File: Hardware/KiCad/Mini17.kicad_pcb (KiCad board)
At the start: 2 copper layers, 160 parts, among them IC1 LM4861M, J1 USB_C, J2 STLink, J3 Micro_SD_Card_Det, J6 UART, J7 OLED, J8 Conn_Coaxial, SW1 PTT, SW10 SW_Push_45deg, SW11 SW_Push_45deg, SW12 SW_Push_45deg, SW13 SW_Push_45deg, SW14 SW_Push_45deg, SW15 SW_Push_45deg, SW16 SW_Push_45deg, SW17 SW_Push_45deg, SW2 SW_Push_45deg, SW3 SW_Push_45deg, SW4 SW_Push_45deg, SW5 SW_Push_45deg, SW6 SW_Push_45deg, SW7 SW_Push_45deg, SW8 SW_Push_45deg, SW9 SW_Push_45deg, U1 USBLC6-2, U3 STM32F427ZGTx, U4 CC1200, U5 MAX9814, U6 TP6841S6, U7 TPS73233, Y1 8 MHz, Y3 40 MHz

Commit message: move cc1200 spi to spi-5 & update other labels throughout
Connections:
- U3 pad 110: CC_NCS -> unconnected-(U3-Pad110)
- U3 pad 133: CC_SCLK -> unconnected-(U3-Pad133)
- U3 pad 134: CC_MISO -> unconnected-(U3-Pad134)
- U3 pad 135: CC_MOSI -> unconnected-(U3-Pad135)
- U3 pad 137: CC_NRST -> unconnected-(U3-Pad137)
- U3 pad 15: unconnected-(U3-Pad15) -> CC_NRST
- U3 pad 18: unconnected-(U3-Pad18) -> CC_NCS
- U3 pad 19: unconnected-(U3-Pad19) -> CC_SCLK
- U3 pad 20: unconnected-(U3-Pad20) -> CC_MISO
- U3 pad 21: unconnected-(U3-Pad21) -> CC_MOSI
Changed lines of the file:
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@@
   (net 119 "unconnected-(U3-Pad13)")
   (net 120 "unconnected-(U3-Pad14)")
-  (net 121 "unconnected-(U3-Pad15)")
-  (net 122 "unconnected-(U3-Pad18)")
-  (net 123 "unconnected-(U3-Pad19)")
-  (net 124 "unconnected-(U3-Pad20)")
-  (net 125 "unconnected-(U3-Pad21)")
+  (net 121 "unconnected-(U3-Pad110)")
+  (net 122 "unconnected-(U3-Pad133)")
+  (net 123 "unconnected-(U3-Pad134)")
+  (net 124 "unconnected-(U3-Pad135)")
+  (net 125 "unconnected-(U3-Pad137)")
   (net 126 "unconnected-(U3-Pad22)")
   (net 127 "unconnected-(U3-Pad26)")
@@
       (net 120 "unconnected-(U3-Pad14)") (pinfunction "PF4") (pintype "bidirectional"))
     (pad "15" smd roundrect (at -10.6625 -1.75) (size 1.475 0.3) (layers "F.Cu" "F.Paste" "F.Mask") (roundrect_rratio 0.25)
-      (net 121 "unconnected-(U3-Pad15)") (pinfunction "PF5") (pintype "bidirectional"))
+      (net 186 "CC_NRST") (pinfunction "PF5") (pintype "bidirectional"))
     (pad "16" smd roundrect (at -10.6625 -1.25) (size 1.475 0.3) (layers "F.Cu" "F.Paste" "F.Mask") (roundrect_rratio 0.25)
       (net 1 "GND") (pinfunction "VSS") (pintype "power_in"))
@@
       (net 20 "VDD") (pinfunction "VDD") (pintype "power_in"))
     (pad "18" smd roundrect (at -10.6625 -0.25) (size 1.475 0.3) (layers "F.Cu" "F.Paste" "F.Mask") (roundrect_rratio 0.25)
-      (net 122 "unconnected-(U3-Pad18)") (pinfunction "PF6") (pintype "bidirectional"))
+      (net 167 "CC_NCS") (pinfunction "PF6") (pintype "bidirectional"))
     (pad "19" smd roundrect (at -10.6625 0.25) (size 1.475 0.3) (layers "F.Cu" "F.Paste" "F.Mask") (roundrect_rratio 0.25)
-      (net 123 "unconnected-(U3-Pad19)") (pinfunction "PF7") (pintype "bidirectional"))
+      (net 182 "CC_SCLK") (pinfunction "PF7") (pintype "bidirectional"))
     (pad "20" smd roundrect (at -10.6625 0.75) (size 1.475 0.3) (layers "F.Cu" "F.Paste" "F.Mask") (roundrect_rratio 0.25)
-      (net 124 "unconnected-(U3-Pad20)") (pinfunction "PF8") (pintype "bidirectional"))
+      (net 183 "CC_MISO") (pinfunction "PF8") (pintype "bidirectional"))
     (pad "21" smd roundrect (at -10.6625 1.25) (size 1.475 0.3) (layers "F.Cu" "F.Paste" "F.Mask") (roundrect_rratio 0.25)
-      (net 125 "unconnected-(U3-Pad21)") (pinfunction "PF9") (pintype "bidirectional"))
+      (net 184 "CC_MOSI") (pinfunction "PF9") (pintype "bidirectional"))
     (pad "22" smd roundrect (at -10.6625 1.75) (size 1.475 0.3) (layers "F.Cu" "F.Paste" "F.Mask") (roundrect_rratio 0.25)
       (net 126 "unconnected-(U3-Pad22)") (pinfunction "PF10") (pintype "bidirectional"))
@@
       (net 74 "SWCLK") (pinfunction "PA14") (pintype "bidirectional"))
     (pad "110" smd roundrect (at 8.25 -10.6625) (size 0.3 1.475) (layers "F.Cu" "F.Paste" "F.Mask") (roundrect_rratio 0.25)
-      (net 167 "CC_NCS") (pinfunction "PA15") (pintype "bidirectional"))
+      (net 121 "unconnected-(U3-Pad110)") (pinfunction "PA15") (pintype "bidirectional"))
     (pad "111" smd roundrect (at 7.75 -10.6625) (size 0.3 1.475) (layers "F.Cu" "F.Paste" "F.Mask") (roundrect_rratio 0.25)
       (net 59 "SD_D2") (pinfunction "PC10") (pintype "bidirectional"))
@@
       (net 181 "unconnected-(U3-Pad132)") (pinfunction "PG15") (pintype "bidirectional"))
     (pad "133" smd roundrect (at -3.25 -10.6625) (size 0.3 1.475) (layers "F.Cu" "F.Paste" "F.Mask") (roundrect_rratio 0.25)
-      (net 182 "CC_SCLK") (pinfunction "PB3") (pintype "bidirectional"))
+      (net 122 "unconnected-(U3-Pad133)") (pinfunction "PB3") (pintype "bidirectional"))
     (pad "134" smd roundrect (at -3.75 -10.6625) (size 0.3 1.475) (layers "F.Cu" "F.Paste" "F.Mask") (roundrect_rratio 0.25)
-      (net 183 "CC_MISO") (pinfunction "PB4") (pintype "bidirectional"))
+      (net 123 "unconnected-(U3-Pad134)") (pinfunction "PB4") (pintype "bidirectional"))
     (pad "135" smd roundrect (at -4.25 -10.6625) (size 0.3 1.475) (layers "F.Cu" "F.Paste" "F.Mask") (roundrect_rratio 0.25)
-      (net 184 "CC_MOSI") (pinfunction "PB5") (pintype "bidirectional"))
+      (net 124 "unconnected-(U3-Pad135)") (pinfunction "PB5") (pintype "bidirectional"))
     (pad "136" smd roundrect (at -4.75 -10.6625) (size 0.3 1.475) (layers "F.Cu" "F.Paste" "F.Mask") (roundrect_rratio 0.25)
       (net 185 "unconnected-(U3-Pad136)") (pinfunction "PB6") (pintype "bidirectional"))
     (pad "137" smd roundrect (at -5.25 -10.6625) (size 0.3 1.475) (layers "F.Cu" "F.Paste" "F.Mask") (roundrect_rratio 0.25)
-      (net 186 "CC_NRST") (pinfunction "PB7") (pintype "bidirectional"))
+      (net 125 "unconnected-(U3-Pad137)") (pinfunction "PB7") (pintype "bidirectional"))
     (pad "138" smd roundrect (at -5.75 -10.6625) (size 0.3 1.475) (layers "F.Cu" "F.Paste" "F.Mask") (roundrect_rratio 0.25)
       (net 187 "~{BOOT0}") (pinfunction "BOOT0") (pintype "input"))

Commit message: starting basic layout
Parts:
- moved J8 118.1 mm to (278.1, 117.0), turned to -90 degrees
- moved H2 106.7 mm to (143.1, 175.0)
- moved H1 106.7 mm to (141.4, 180.4)
- moved H3 106.7 mm to (151.3, 167.1)
- moved H4 106.7 mm to (135.8, 183.3)
- moved J3 105.8 mm to (66.3, 188.9)
- moved C51 105.2 mm to (267.7, 118.0), turned to 180 degrees
- moved C54 103.8 mm to (272.2, 118.4), turned to -90 degrees
- moved R29 103.2 mm to (265.2, 120.2), turned to 90 degrees
- moved L9 100.6 mm to (272.6, 117.0)
- moved L8 99.7 mm to (270.7, 117.0)
- moved L7 99.4 mm to (267.7, 117.0)
- moved L6 99.0 mm to (264.2, 117.5), turned to 90 degrees
- moved C50 95.9 mm to (264.2, 120.1), turned to 90 degrees
- moved C27 95.1 mm to (220.9, 36.9)
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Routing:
- net CC_X1: track 0.00 -> 9.32 mm
- net CC_X2: track 0.00 -> 6.42 mm
- net GND: track 0.00 -> 3.70 mm

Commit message: rough layout of cc1200
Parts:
- added C11: 47n, Capacitor_SMD:C_0402_1005Metric, F.Cu at (238.9, 113.0)
- added C121: 47n, Capacitor_SMD:C_0402_1005Metric, F.Cu at (243.7, 121.3)
- added C131: 47n, Capacitor_SMD:C_0402_1005Metric, F.Cu at (244.8, 121.3)
- added C151: 47n, Capacitor_SMD:C_0402_1005Metric, F.Cu at (245.9, 120.2)
- added C221: 47n, Capacitor_SMD:C_0402_1005Metric, F.Cu at (251.3, 112.4)
- added C251: 47n, Capacitor_SMD:C_0402_1005Metric, F.Cu at (248.1, 109.5)
- added C271: 47n, Capacitor_SMD:C_0402_1005Metric, F.Cu at (246.1, 109.5)
- added C281: 47n, Capacitor_SMD:C_0402_1005Metric, F.Cu at (245.0, 109.5)
- added C51: 47n, Capacitor_SMD:C_0402_1005Metric, F.Cu at (238.9, 115.0)
- moved R171 16.8 mm to (248.5, 119.0), turned to 0 degrees
- moved L172 14.7 mm to (253.0, 116.5), turned to 90 degrees
- moved C174 14.2 mm to (251.5, 117.0)
- moved L171 14.2 mm to (250.0, 117.5), turned to -90 degrees
- moved C173 14.2 mm to (250.1, 119.5)
- moved C176 13.2 mm to (254.5, 117.0)
- moved C175 13.2 mm to (259.0, 117.4)
- moved C181 13.2 mm to (256.0, 116.6)
- moved L173 13.2 mm to (257.5, 117.0)
- moved L174 12.1 mm to (260.5, 117.0)
- moved J8 11.6 mm to (266.5, 117.0)
- moved C172 6.15 mm to (248.0, 120.5), turned to -90 degrees
- moved C301 3.48 mm to (241.3, 107.5), turned to 0 degrees
- moved L192 3.11 mm to (256.4, 113.1), turned to 0 degrees
- moved C291 2.86 mm to (244.1, 108.5), turned to -90 degrees
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- renumbered C52 to C171, C55 to C172, C50 to C173, C49 to C174, C54 to C175, C51 to C176, C53 to C181, C47 to C191, C48 to C201, C13 to C211, C10 to C231, C12 to C261, C11 to C291, C8 to C301, C9 to C311, C14 to C61, C61 to C9, L6 to L171, L7 to L172, L8 to L173, L9 to L174, L3 to L191, L2 to L192, L5 to L193, L4 to L201, R9 to R141, R29 to R171
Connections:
- C173 pad 2: Net-(C50-Pad2) -> Net-(C173-Pad2)
- L171 pad 1: Net-(C50-Pad2) -> PA
- L171 pad 2: PA -> Net-(C173-Pad2)
- R171 pad 2: Net-(C50-Pad2) -> Net-(C173-Pad2)
- U3 pad 6: +BATT -> VBAT
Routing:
- net VDD: track 0.00 -> 31.6 mm
- net GND: track 3.70 -> 20.9 mm
- net LNA_N: track 0.00 -> 10.2 mm
- net TRX_SW: track 0.00 -> 9.83 mm
- net LNA_P: track 0.00 -> 9.73 mm
- net CC_X1: track 9.32 -> 0.00 mm
- net Net-(C191-Pad2): track 0.00 -> 7.65 mm
- net CC_X2: track 6.42 -> 0.00 mm
- net Net-(J8-Pad1): track 0.00 -> 5.53 mm
- net Net-(C176-Pad1): track 0.00 -> 4.71 mm
- net Net-(C211-Pad1): track 0.00 -> 3.66 mm
- net Net-(C61-Pad1): track 0.00 -> 3.63 mm
- net Net-(C231-Pad2): track 0.00 -> 3.19 mm
- net PA: track 0.00 -> 3.17 mm
- net Net-(C261-Pad1): track 0.00 -> 3.01 mm
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
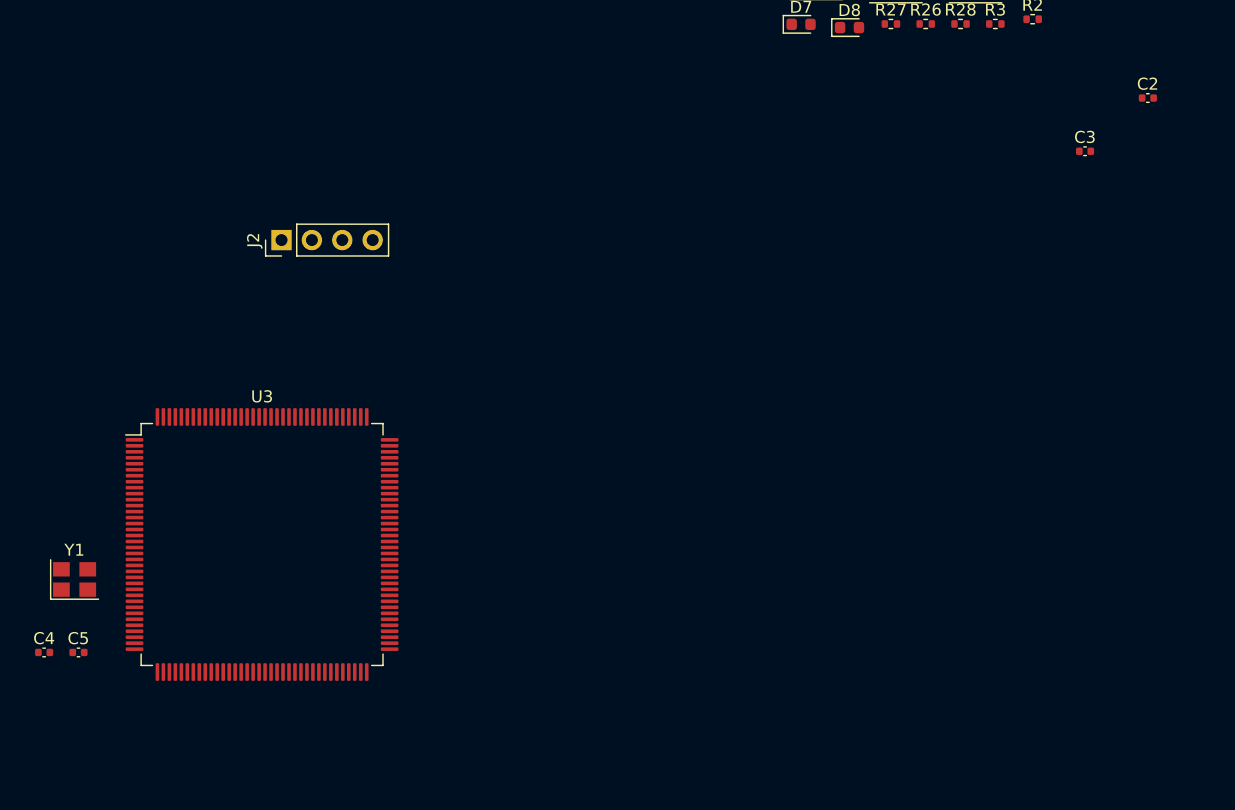
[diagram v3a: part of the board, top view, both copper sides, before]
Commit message: fix issue 21 & 20 & move MCU to align w/ grid
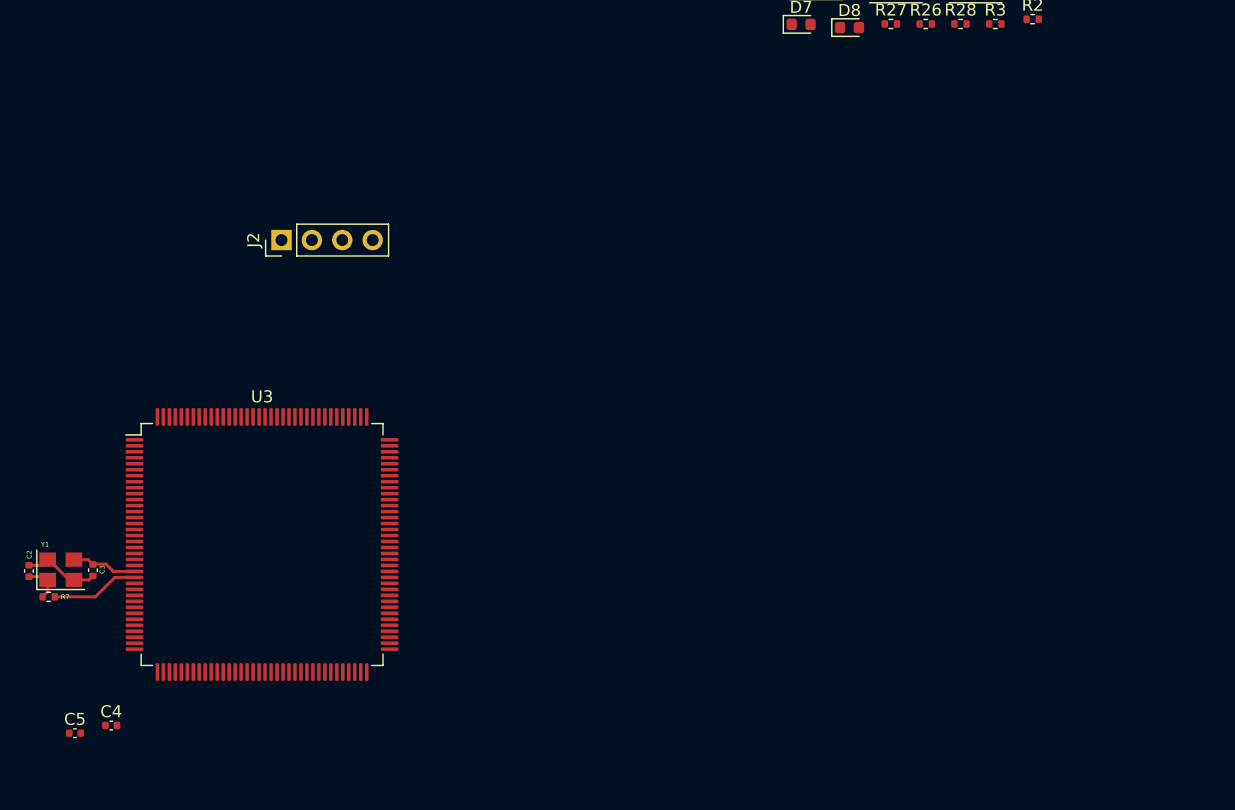
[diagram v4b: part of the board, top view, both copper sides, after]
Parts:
- added R7: 0, Resistor_SMD:R_0402_1005Metric, F.Cu at (15.9, 136.7)
- moved C2 101.6 mm to (14.2, 134.5), turned to -90 degrees
- moved C3 90.0 mm to (19.6, 134.4), turned to -90 degrees
- moved C4 8.29 mm to (21.1, 147.4)
- moved C5 6.76 mm to (18.1, 148.1)
- moved Y1 1.41 mm to (16.9, 134.4)
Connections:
- C2 pad 2: XTAL_1 -> Net-(C2-Pad2)
- Y1 pad 1: XTAL_1 -> Net-(C2-Pad2)
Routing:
- net XTAL_1: track 0.00 -> 7.34 mm
- net GND: track 20.9 -> 27.3 mm
- net XTAL_2: track 0.00 -> 5.50 mm
- net Net-(C2-Pad2): track 0.00 -> 3.26 mm

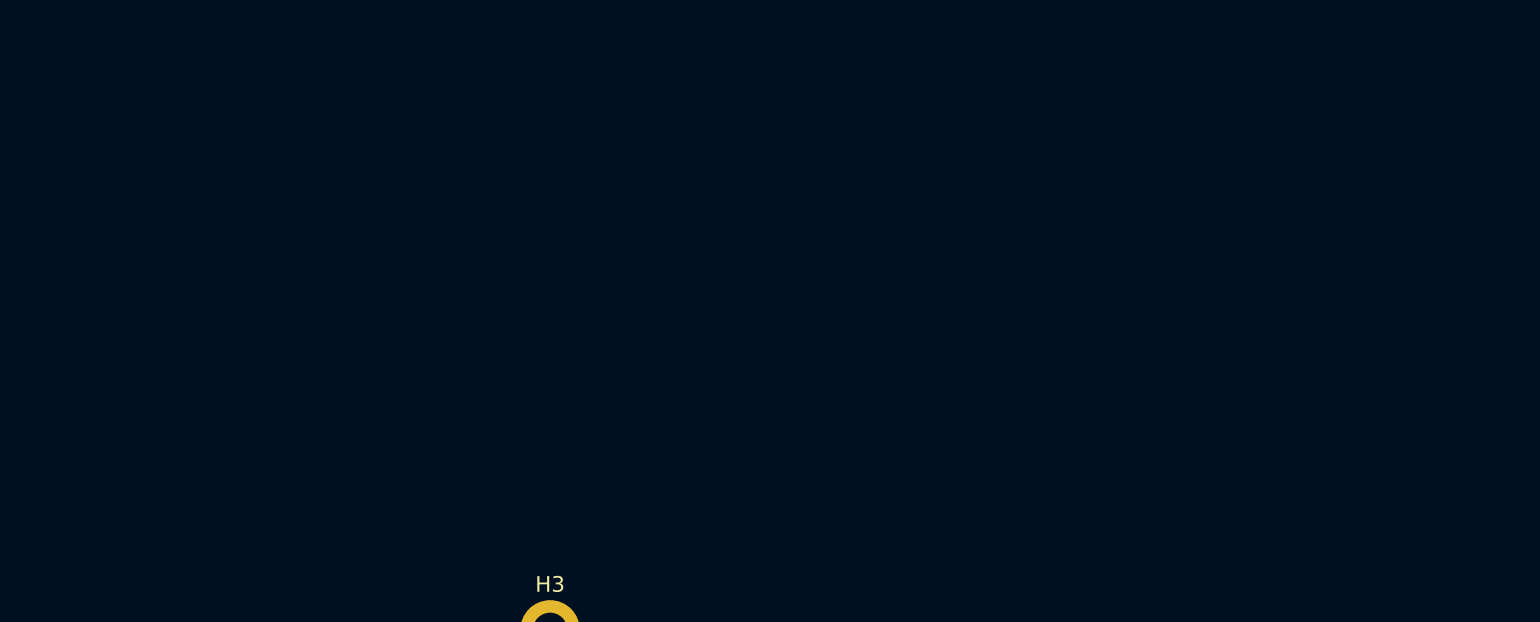
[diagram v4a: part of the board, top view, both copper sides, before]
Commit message: fixup PTT/Audio (Issue 14), add RGB LED (Issue 26), Connect LEDs to MCU & add them to the .ioc file
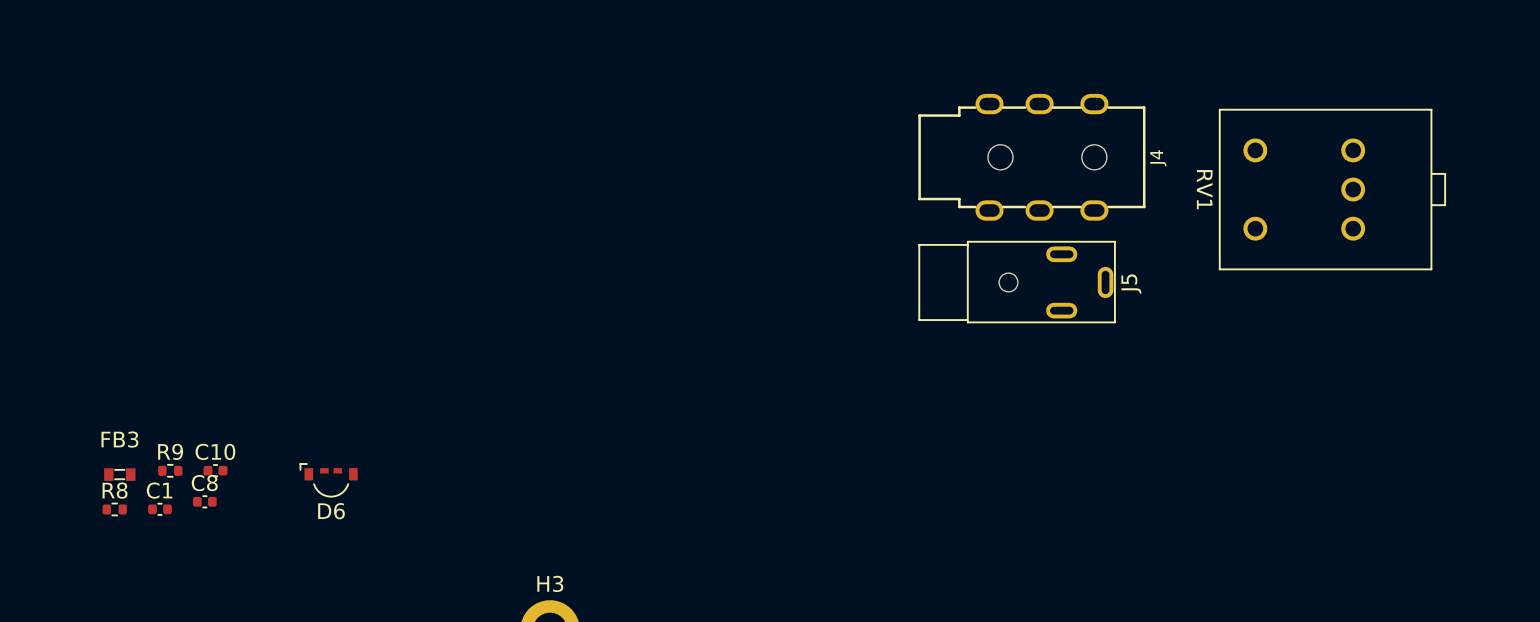
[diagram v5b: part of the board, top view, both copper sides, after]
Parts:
- added C1: 220n, Capacitor_SMD:C_0402_1005Metric, F.Cu at (126.4, 159.4)
- added C10: 220n, Capacitor_SMD:C_0402_1005Metric, F.Cu at (129.9, 156.9)
- added C8: 4.7u, Capacitor_SMD:C_0402_1005Metric, F.Cu at (129.3, 158.9)
- added D6: 12-23C/R6GHBHC-A01/2C, LED_SMD:LED_RGB_Everlight_EASV3015RGBA0_Horizontal, F.Cu at (137.3, 157.7)
- added FB3: BLM18AG601SN1D, digikey-footprints:0603, F.Cu at (123.8, 157.2)
- added J4: Kenwood-3.5, M17-SmartMic:PJ-3136-B, F.Cu at (177.6, 136.9)
- added J5: Kenwood-2.5, M17-SmartMic:PJ-211A, F.Cu at (180.6, 144.9)
- added R8: 470, Resistor_SMD:R_0402_1005Metric, F.Cu at (123.5, 159.4)
- added R9: 1k8, Resistor_SMD:R_0402_1005Metric, F.Cu at (127.0, 156.9)
- added RV1: 50k, M17-SmartMic:PTR901, F.Cu at (199.5, 138.9)
- R7: value 0 -> 0R
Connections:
- C27 pad 2: SPEAKER -> EXT_SPEAKER
- LS1 pad 1: SPEAKER -> INT_SPEAKER
- R25 pad 2: unconnected-(R25-Pad2) -> VDD
- TP4 pad 1: SPEAKER -> EXT_SPEAKER
- U3 pad 41: unconnected-(U3-Pad41) -> LED-PTT
- U3 pad 5: unconnected-(U3-Pad5) -> LED-SYNC
- U3 pad 81: unconnected-(U3-Pad81) -> LED-ERROR
